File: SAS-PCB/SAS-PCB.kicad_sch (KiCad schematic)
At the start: 25 parts, among them J10-FTDI1 Conn_01x06, J10-FTDI2 Conn_01x06, J1_Batt1 691137710002, J2-LCD1 Conn_01x04_Socket, J3-LCD2 Conn_01x04_Socket, J4-BMP280 Conn_01x06_Pin, J5-GPS1 Conn_01x04_Socket, J6-cable-plat1 Conn_02x20_Odd_Even, J7-RFD900x1 691137710002, J8-Fan1 Conn_01x04_Socket, J9-Fan2 Conn_01x04_Socket

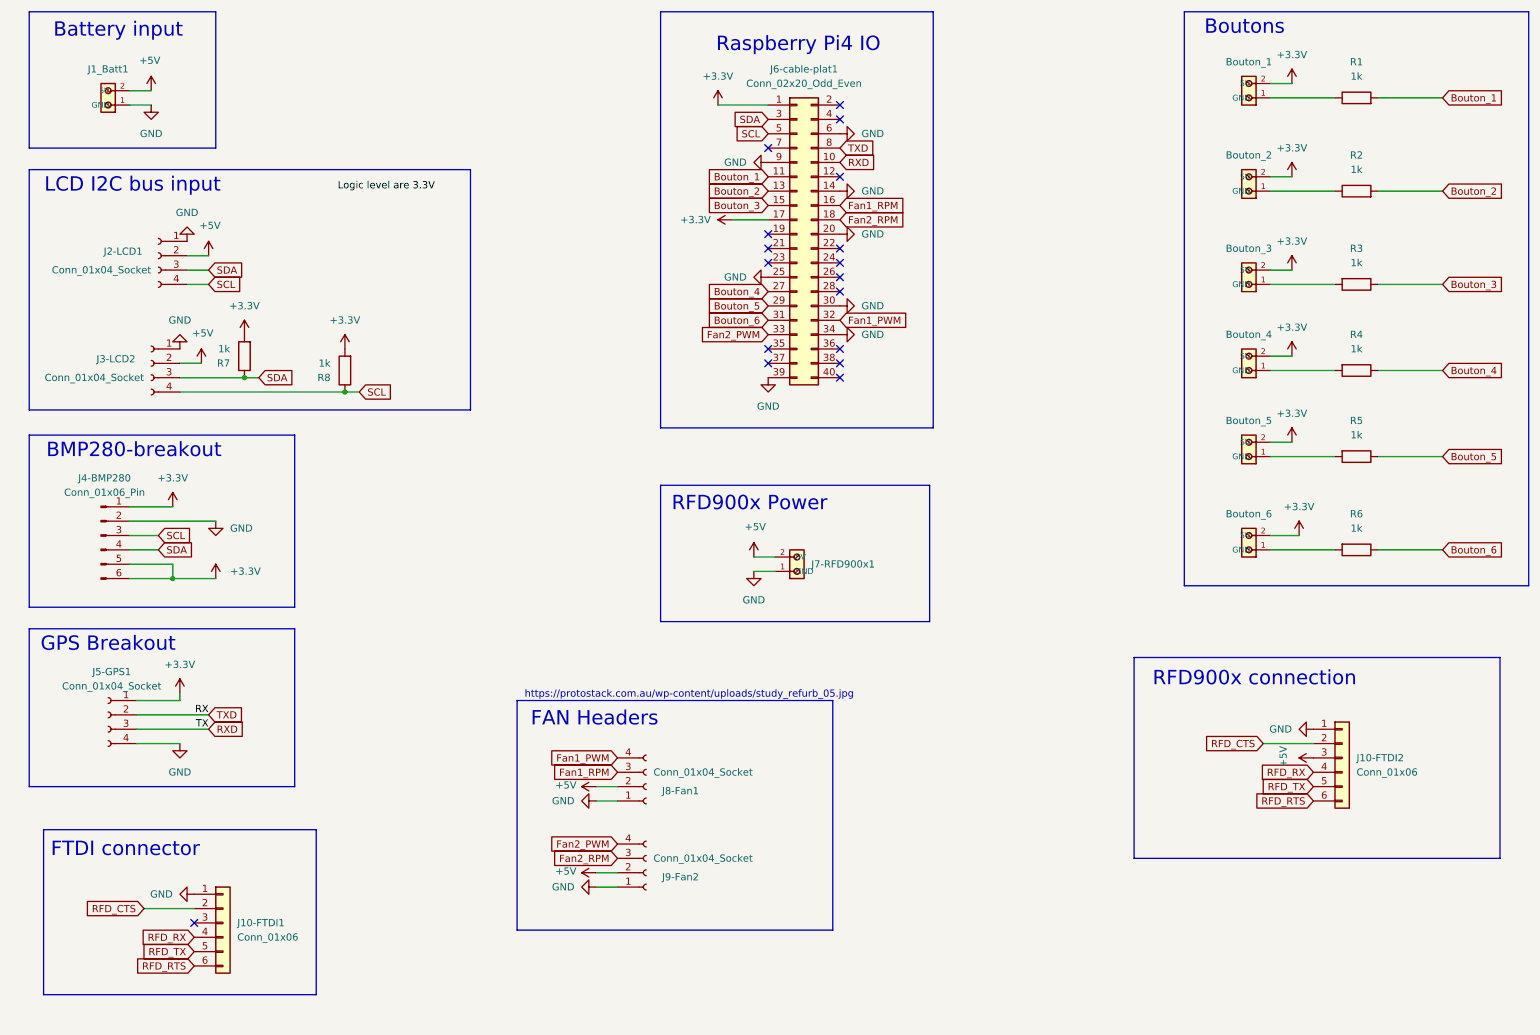
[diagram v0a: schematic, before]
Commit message: A_verifier_demain
Abandon du RPM tachymetre pour le mieux.
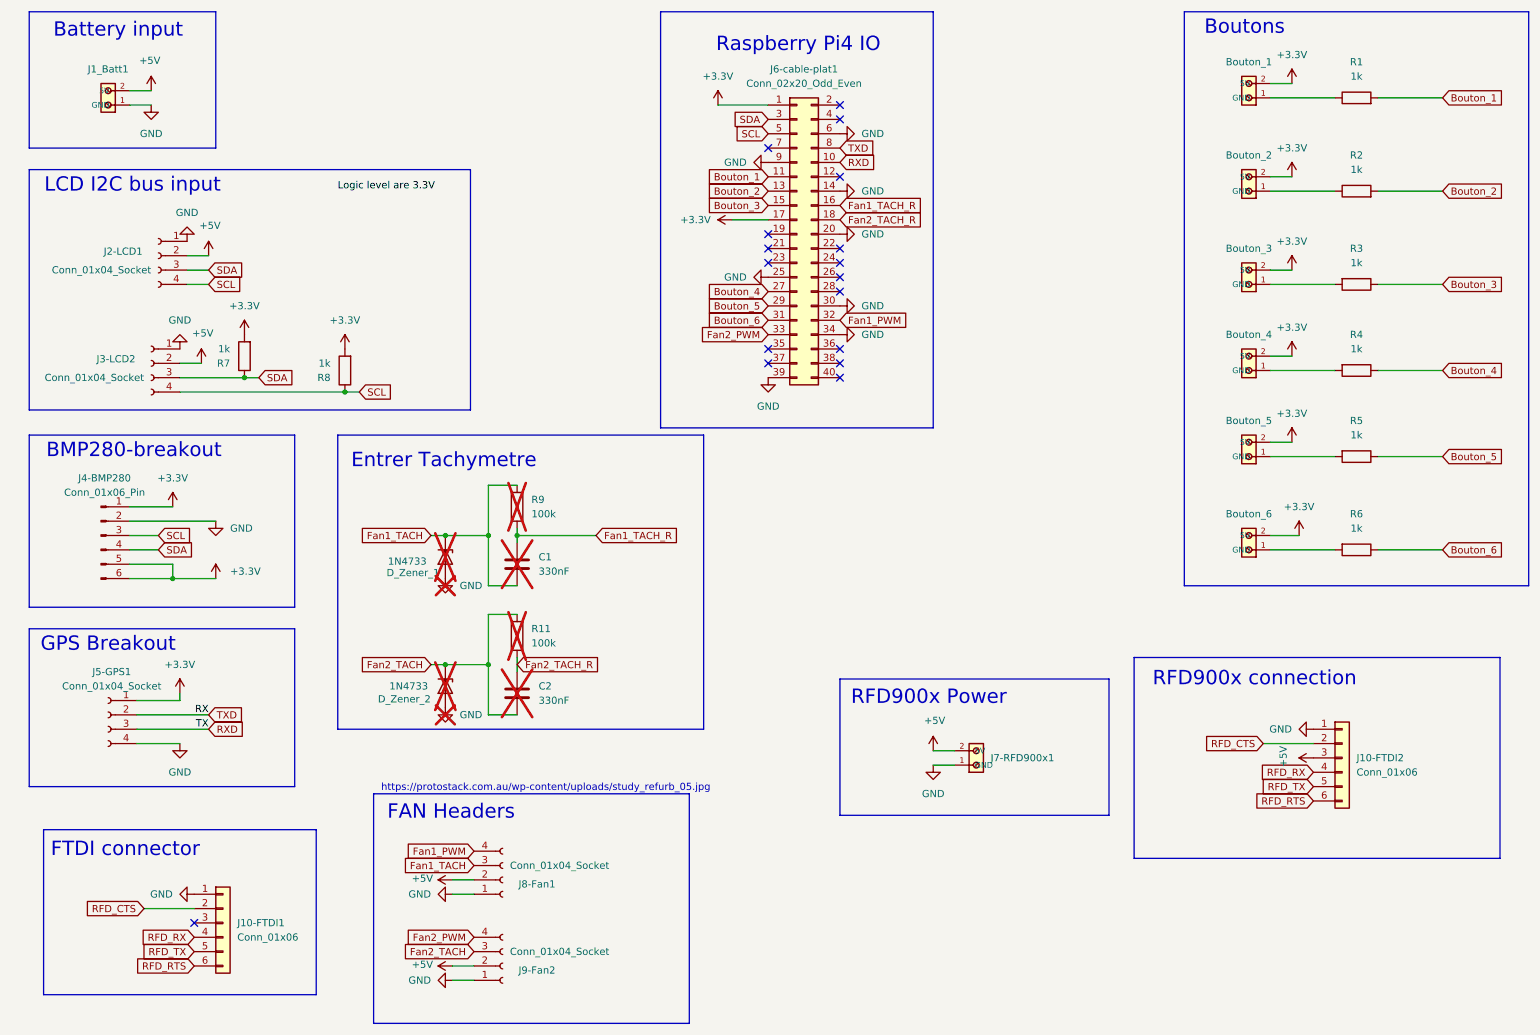
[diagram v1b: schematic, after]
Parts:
- added C1, C2: 330nF, SAS-Librarie-Empreinte:C_Axial_L3.8mm_D2.6mm_P7.50mm_Horizontal, symbol Device:C
- added D_Zener_1, D_Zener_2: 1N4733, SAS-Librarie-Empreinte:D_DO-41_SOD81_P10.16mm_Horizontal, symbol Device:D_Zener
- added R11, R9: 100k, SAS-Librarie-Empreinte:Resistance, symbol Device:R
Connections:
- net GND: now also D_Zener_1.2 (A), D_Zener_2.2 (A)
- net Fan1_RPM renamed Fan1_TACH
- net Fan1_TACH: now also C1.2, D_Zener_1.1 (K), R9.2; no longer J6-cable-plat1.16 (Pin_16)
- net Fan2_RPM renamed Fan2_TACH
- net Fan2_TACH: now also C2.2, D_Zener_2.1 (K), R11.2; no longer J6-cable-plat1.18 (Pin_18)
- new net Fan1_TACH_R: C1.1, J6-cable-plat1.16 (Pin_16), R9.1
- new net Fan2_TACH_R: C2.1, J6-cable-plat1.18 (Pin_18), R11.1
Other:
- note added: "Entrer Tachymetre"
- moved on the sheet: J7-RFD900x1, J8-Fan1, J9-Fan2
